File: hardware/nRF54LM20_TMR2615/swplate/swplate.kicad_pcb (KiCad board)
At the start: 2 copper layers, 313.9 x 198.7 mm, 103 parts, among them M1 Minew_ME54BS13_V1.0

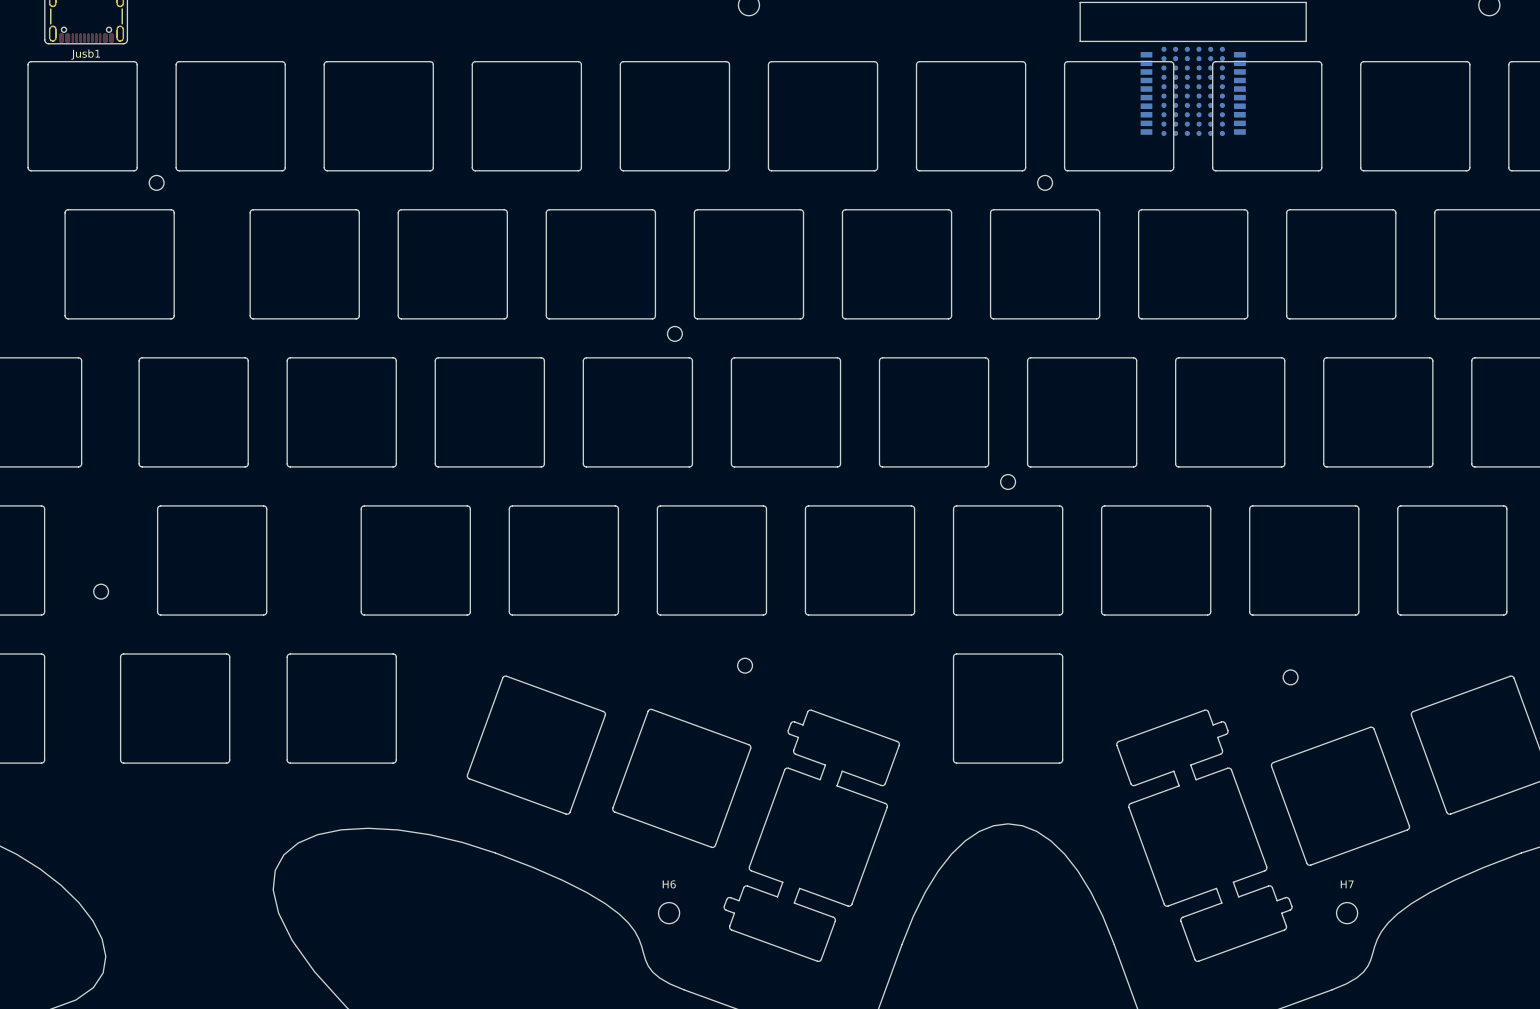
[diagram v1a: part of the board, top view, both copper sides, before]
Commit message: M  hardware/nRF54LM20_TMR2615/pcb/pcb.kicad_pcb M  hardware/nRF54LM20_TMR2615/pcb/pcb.kicad_prl M  hardware/nRF54LM20_TMR2615/swplate/swplate.kicad_pcb M  hardware/nRF54LM20_TMR2615/swplate/swplate.kicad_pro M  hardware/nRF54LM20_TMR2615/swplate/swplate.kicad_sch A  hardware/nRF54LM20_TMR2615/tmr-footprints/SW_CK_PTS530_4.5x4.5x0.55mm_holeonly.kicad_mod
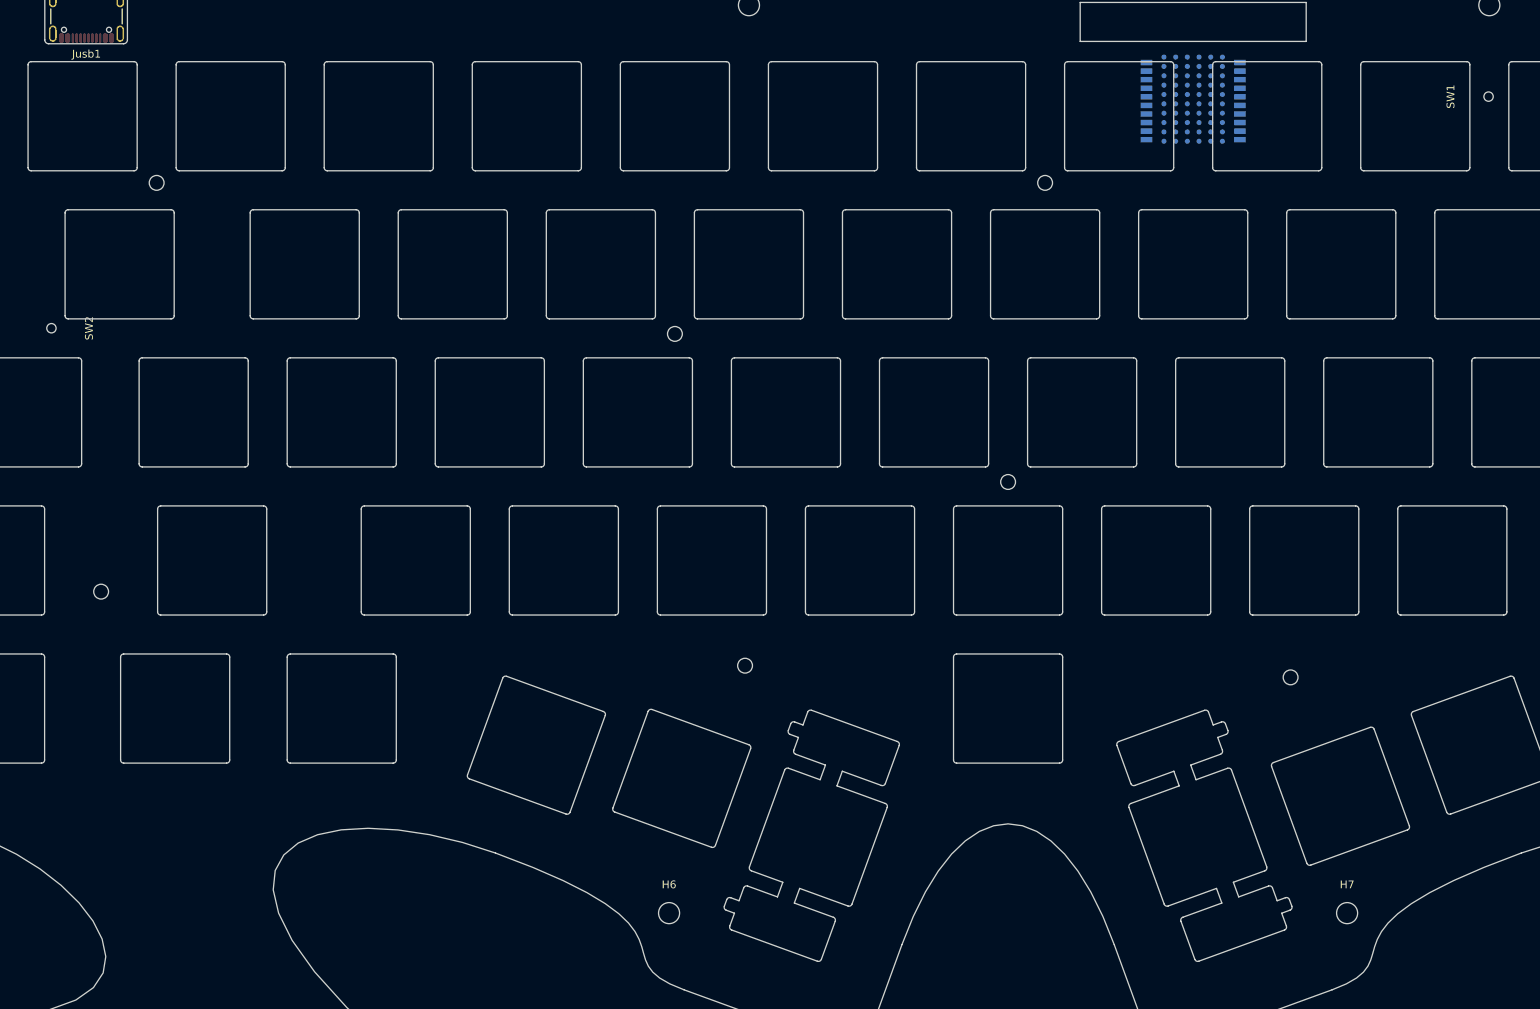
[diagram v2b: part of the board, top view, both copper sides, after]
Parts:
- added SW1: SW_Hole, tmr-lib:SW_CK_PTS530_4.5x4.5x0.55mm_holeonly, F.Cu at (199.4, -2.52)
- added SW2: SW_Hole, tmr-lib:SW_CK_PTS530_4.5x4.5x0.55mm_holeonly, F.Cu at (15.0, 27.2)
- moved M1 1.00 mm to (167.6, 4.20)

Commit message: M  hardware/nRF54LM20_TMR2615/swplate/swplate.kicad_pcb M  hardware/nRF54LM20_TMR2615/swplate/swplate.kicad_sch A  hardware/nRF54LM20_TMR2615/tmr-footprints/MountingHole_3.2mm_M3_Heatsink_3.6mm.kicad_mod
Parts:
- H1, H10, H11, H12, H13, H14, H15, H16, H2, H3, H4, H5, H6, H7, H8, H9: footprint tmr-lib:MountingHole_2.7mm_M2.5 -> tmr-lib:MountingHole_3.2mm_M3_Heatsink_3.6mm
- SW1, SW2: moved to B.Cu
- moved H10 3.57 mm to (66.5, 127.5)
- moved H14 3.57 mm to (209.1, 127.5)
- moved H2 1.00 mm to (104.5, -15.2)
- moved H3 1.00 mm to (199.5, -15.2)
- moved H4 1.00 mm to (291.0, -15.2)
- moved H9 0.99 mm to (-6.95, 122.8)
- moved H11 0.99 mm to (66.5, 173.2)
- moved H13 0.99 mm to (287.4, 122.8)
- moved H12 0.99 mm to (-6.95, 173.2)
- moved H15 0.99 mm to (209.1, 173.2)
- moved H16 0.99 mm to (287.4, 173.2)
- moved H6 0.90 mm to (93.5, 102.8)
- moved H7 0.90 mm to (182.0, 102.8)
- moved Hd1 0.75 mm to (4.55, -5.20)
- moved H5 0.60 mm to (-10.3, 71.0)
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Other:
- board size 313.9 x 198.7 mm -> 316.4 x 200.6 mm
